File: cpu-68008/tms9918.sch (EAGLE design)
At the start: 45 parts, among them IC101 74HCT245, IC102 74HCT245, IC103 74HCT245, IC104 74HCT245, IC201 GAL22V10D

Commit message: added /DS to GALs on all peripherals and backplane began work on TMS9918 video card
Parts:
- removed C105, C107, C202, C301, C302, C303, C304: 100nF, rcl:C-EUC0805
- removed C106, C201, C305, C306: 10µF, rcl:CPOL-EUSMCB
- removed H101, H102, H103, H104: MOUNT-HOLE2.8, holes:MOUNT-HOLE2.8
- removed IC102, IC103, IC104: 74HCT245, 74xx-eu:74HCT245DW
- removed IC201: GAL22V10D, 68komputer:GAL22V10DIP24
- removed LED101, LED301, LED302, LED303, LED304: (no value), led:LEDCHIPLED_1206
- removed R101, R102: 10k, rcl:R-EU_R2012
- removed R103, R301, R302, R303, R304: 3k, rcl:R-EU_R2012
- removed SV102: (no value), con-lstb:MA20-2
- removed SV103: (no value), con-lstb:MA10-2W
- removed SV104: (no value), con-lstb:MA20-2W
- removed SV301, SV302, SV303, SV304: (no value), con-lsta:FE20-2
- removed WEED301: WEED, 68komputer:WEED
- added C1, C6: 10µF, rcl:CPOL-EUSMCB
- added C2, C3, C4, C5, C7: 100nF, rcl:C-EUC0805
- added IC1, IC2, IC3: 74HCT574N, 74xx-eu:74HCT574N
- added IC4: 74HCT04N, 74xx-eu:74HCT04N
- added IC5: AS6C62256, 68komputer:AS6C62256
- added LED201: (no value), led:LEDCHIPLED_1206
- added R201: 10k, rcl:R-EU_R2012
- added R202: 3k, rcl:R-EU_R2012
- C102: value 47µF -> 10µF; device rcl:CPOL-EUE2-5 -> rcl:CPOL-EUSMCB; MOUSER 710-860020472006 -> 581-TAJB106K020RNJV
- C104: value 100nF -> 10µF; device rcl:C-EUC0805 -> rcl:CPOL-EUSMCB; MOUSER 710-885012207072 -> 581-TAJB106K020RNJV
- IC101: value 74HCT245 -> GAL22V10D; device 74xx-eu:74HCT245DW -> 68komputer:GAL22V10DIP24; MOUSER_SOCKET (none) -> 575-11044324
- SV101: device con-lstb:MA10-2 -> con-lstb:MA20-2W
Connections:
- removed net !AS: IC104A.A1, SV102.33, SV104.33
- removed net !BERR: SV102.9, SV104.9
- removed net !BG: SV102.25, SV104.25
- removed net !BR: SV102.23, SV104.23
- removed net !BUF_ADDR_OE: IC102A.G, IC103A.G, IC201.IO17
- removed net !BUF_DATA_OE: IC101A.G, IC201.IO16
- removed net !BUS_CS: IC201.IN2, SV101.7, SV103.7
- removed net !BUS_DTACK: IC201.IO14, SV101.6, SV103.6
- removed net !DS: IC104A.A2, SV102.31, SV104.31
- removed net !DTACK: SV102.27, SV104.27
- removed net !HALT: SV102.17, SV104.17
- removed net !RESET: IC104A.A8, SV102.15, SV104.15
- removed net !SLOT_CS0: IC201.IO23, LED301.C, SV301.5
- removed net !SLOT_CS1: IC201.IO22, LED302.C, SV303.5
- removed net !SLOT_CS2: IC201.IO21, LED303.C, SV302.5
- removed net !SLOT_CS3: IC201.IO20, LED304.C, SV304.5
- removed net !VPA: SV102.11, SV104.11
- removed net A0: IC102A.A4, SV101.17, SV103.17
- removed net A1: IC102A.A6, SV101.15, SV103.15
- removed net A10: IC103A.A6, SV102.8, SV104.8
- removed net A11: IC103A.A5, SV102.10, SV104.10
- removed net A12: IC103A.A4, SV102.12, SV104.12
- removed net A13: IC103A.A3, SV102.14, SV104.14
- removed net A14: IC103A.A2, SV102.16, SV104.16
- removed net A15: IC103A.A1, SV102.20, SV104.20
- removed net A16: IC104A.A7, SV102.24, SV104.24
- removed net A17: IC104A.A6, SV102.26, SV104.26
- removed net A18: IC104A.A5, SV102.28, SV104.28
- removed net A19: IC104A.A3, SV102.30, SV104.30
- removed net A2: IC102A.A8, SV101.13, SV103.13
- removed net A3: IC102A.A7, SV101.14, SV103.14
- removed net A4: IC102A.A5, SV101.16, SV103.16
- removed net A5: IC102A.A3, SV101.18, SV103.18
- removed net A6: IC102A.A2, SV101.20, SV103.20
- removed net A7: IC102A.A1, SV102.2, SV104.2
- removed net A8: IC103A.A8, SV102.4, SV104.4
- removed net A9: IC103A.A7, SV102.6, SV104.6
- removed net BUF_DATA_DIR: IC101A.DIR, IC201.IO15
- removed net CLK: IC201.IN1/CLK, SV102.21, SV104.21
- removed net D0: IC101A.A6, SV102.35, SV104.35
- removed net D1: IC101A.A4, SV102.37, SV104.37
- removed net D2: IC101A.A2, SV102.39, SV104.39
- removed net D3: IC101A.A1, SV102.40, SV104.40
- removed net D4: IC101A.A3, SV102.38, SV104.38
- removed net D5: IC101A.A5, SV102.36, SV104.36
- removed net D6: IC101A.A7, SV102.34, SV104.34
- removed net D7: IC101A.A8, SV102.32, SV104.32
- removed net E: SV102.13, SV104.13
- removed net FC0: SV101.19, SV103.19
- removed net FC1: SV102.1, SV104.1
- removed net FC2: SV102.3, SV104.3
- removed net N$14: IC201.IN10
- removed net N$15: IC201.IN11
- removed net N$20: IC201.IO19
- removed net N$27: IC201.IO18
- removed net N$3: LED304.A, R304.2
- removed net N$4: LED101.A, R103.2
- removed net N$5: LED303.A, R303.2
- removed net R/!W!: IC104A.A4, SV102.29, SV104.29
- removed net SLOT_A16: IC104A.B7, IC201.IN3
- removed net SLOT_A17: IC104A.B6, IC201.IN4
- removed net SLOT_A18: IC104A.B5, IC201.IN5
- removed net SLOT_A19: IC104A.B3, IC201.IN7
- new net !ATA_ACTY: LED201.C
- new net !ATA_IRQ: R201.1
- new net !SLOT_CS: IC101.IN13, SV101.5
- new net !TMS_CAS: IC4C.I, IC5.!CS
- new net !TMS_RAS: IC4B.I
- new net !TMS_RD: IC1A.CLK, IC4A.O, IC4F.I, IC5.!OE
- new net !TMS_WR: IC4F.O
- new net COL: IC3A.CLK, IC4E.O
- new net N$7: LED201.A, R202.2
- new net ROW: IC2A.CLK, IC4B.O
- new net TMS_AD0: IC1A.1D, IC2A.1D, IC3A.1D
- new net TMS_AD1: IC1A.2D, IC2A.2D, IC3A.2D
- new net TMS_AD2: IC1A.3D, IC2A.3D, IC3A.3D
- new net TMS_AD3: IC1A.4D, IC2A.4D, IC3A.4D
- new net TMS_AD4: IC1A.5D, IC2A.5D, IC3A.5D
- new net TMS_AD5: IC1A.6D, IC2A.6D, IC3A.6D
- new net TMS_AD6: IC1A.7D, IC2A.7D, IC3A.7D
- new net TMS_AD7: IC1A.8D, IC2A.8D, IC3A.8D
- new net TMS_R/!W!: IC1A.OC, IC4A.I, IC5.!WE
- new net TMS_VD0: IC1A.1Q, IC5.DQ0
- new net TMS_VD1: IC1A.2Q, IC5.DQ1
- new net TMS_VD2: IC1A.3Q, IC5.DQ2
- new net TMS_VD3: IC1A.4Q, IC5.DQ3
- new net TMS_VD4: IC1A.5Q, IC5.DQ4
- new net TMS_VD5: IC1A.6Q, IC5.DQ5
- new net TMS_VD6: IC1A.7Q, IC5.DQ6
- new net TMS_VD7: IC1A.8Q, IC5.DQ7
- new net VRAM_A0: IC2A.2Q, IC5.A0
- new net VRAM_A1: IC2A.3Q, IC5.A1
- new net VRAM_A10: IC3A.5Q, IC5.A10
- new net VRAM_A11: IC3A.6Q, IC5.A11
- new net VRAM_A12: IC3A.7Q, IC5.A12
- new net VRAM_A13: IC3A.8Q, IC5.A13
- new net VRAM_A2: IC2A.4Q, IC5.A2
- new net VRAM_A3: IC2A.5Q, IC5.A3
- new net VRAM_A4: IC2A.6Q, IC5.A4
- new net VRAM_A5: IC2A.7Q, IC5.A5
- new net VRAM_A6: IC2A.8Q, IC5.A6
- new net VRAM_A7: IC3A.2Q, IC5.A7
- new net VRAM_A8: IC3A.3Q, IC5.A8
- new net VRAM_A9: IC3A.4Q, IC5.A9
- new net VRAM_BANK: IC5.A14
- net !BUS_IRQ: now also IC101.IO15, SV101.6; no longer R101.1, SV101.5, SV103.5, SV301.6, SV302.6, SV303.6, SV304.6
- net !SLOT_ACK: now also IC101.IO14, SV101.24; no longer IC201.IN13, R102.1, SV301.24, SV302.24, SV303.24, SV304.24
- net !SLOT_AS: now also IC101.IN7, SV101.32; no longer IC104A.B1, SV301.32, SV302.32, SV303.32, SV304.32
- net !SLOT_DS: now also IC101.IN6, SV101.31; no longer IC104A.B2, IC201.IN9, SV301.31, SV302.31, SV303.31, SV304.31
- net !SLOT_RESET: now also IC101.IN8, SV101.30; no longer IC104A.B8, IC201.IN8, SV301.30, SV302.30, SV303.30, SV304.30
- net +5V: now also C1.+, C104.+, C2.1, C3.1, C4.1, C5.1, C6.+, C7.1, IC101.VCC, IC1P.VCC, IC2P.VCC, IC3P.VCC, IC4P.VCC, IC5.VCC, R201.2, R202.1; no longer C104.1, C105.1, C106.+, C107.1, C201.+, C202.1, C301.1, C302.1, C303.1, C304.1, C305.+, C306.+, IC101P.VCC, IC102A.DIR, IC102P.VCC, IC103A.DIR, IC103P.VCC, IC104A.DIR, IC104P.VCC, IC201.VCC, R101.2, R102.2, R103.1, R301.1, R302.1, R303.1, R304.1, SV103.1, SV103.2, SV301.1, SV301.2, SV302.1, SV302.2, SV303.1, SV303.2, SV304.1, SV304.2
- net GND: now also C1.-, C104.-, C2.2, C3.2, C4.2, C5.2, C6.-, C7.2, IC101.GND, IC1P.GND, IC2A.OC, IC2P.GND, IC3A.OC, IC3P.GND, IC4P.GND, IC5.GND, SV101.25, SV101.26, SV101.27, SV101.28; no longer C104.2, C105.2, C106.-, C107.2, C201.-, C202.2, C301.2, C302.2, C303.2, C304.2, C305.-, C306.-, IC101P.GND, IC102P.GND, IC103P.GND, IC104A.G, IC104P.GND, IC201.GND, LED101.C, SV101.10, SV101.11, SV101.12, SV101.8, SV101.9, SV102.18, SV102.19, SV102.22, SV102.5, SV102.7, SV103.10, SV103.11, SV103.12, SV103.3, SV103.4, SV103.8, SV103.9, SV104.18, SV104.19, SV104.22, SV104.5, SV104.7, SV301.25, SV301.26, SV301.27, SV301.28, SV301.3, SV301.4, SV302.25, SV302.26, SV302.27, SV302.28, SV302.3, SV302.4, SV303.25, SV303.26, SV303.27, SV303.28, SV303.3, SV303.4, SV304.25, SV304.26, SV304.27, SV304.28, SV304.3, SV304.4
- net N$1: now also IC4D.O, IC4E.I; no longer LED302.A, R302.2
- net N$2: now also IC4C.O, IC4D.I; no longer LED301.A, R301.2
- net SLOT_A0: now also SV101.12; no longer IC102A.B4, SV301.12, SV302.12, SV303.12, SV304.12
- net SLOT_A1: now also SV101.10; no longer IC102A.B6, SV301.10, SV302.10, SV303.10, SV304.10
- net SLOT_A10: now also SV101.18; no longer IC103A.B6, SV301.18, SV302.18, SV303.18, SV304.18
- net SLOT_A11: now also SV101.17; no longer IC103A.B5, SV301.17, SV302.17, SV303.17, SV304.17
- net SLOT_A12: now also SV101.20; no longer IC103A.B4, SV301.20, SV302.20, SV303.20, SV304.20
- net SLOT_A13: now also SV101.19; no longer IC103A.B3, SV301.19, SV302.19, SV303.19, SV304.19
- net SLOT_A14: now also SV101.22; no longer IC103A.B2, SV301.22, SV302.22, SV303.22, SV304.22
- net SLOT_A15: now also SV101.21; no longer IC103A.B1, SV301.21, SV302.21, SV303.21, SV304.21
- net SLOT_A2: now also SV101.8; no longer IC102A.B8, SV301.8, SV302.8, SV303.8, SV304.8
- net SLOT_A3: now also SV101.7; no longer IC102A.B7, SV301.7, SV302.7, SV303.7, SV304.7
- net SLOT_A4: now also IC101.IN10, SV101.9; no longer IC102A.B5, SV301.9, SV302.9, SV303.9, SV304.9
- net SLOT_A5: now also IC101.IN11, SV101.11; no longer IC102A.B3, SV301.11, SV302.11, SV303.11, SV304.11
- net SLOT_A6: now also SV101.14; no longer IC102A.B2, SV301.14, SV302.14, SV303.14, SV304.14
- net SLOT_A7: now also SV101.13; no longer IC102A.B1, SV301.13, SV302.13, SV303.13, SV304.13
- net SLOT_A8: now also SV101.16; no longer IC103A.B8, SV301.16, SV302.16, SV303.16, SV304.16
- net SLOT_A9: now also SV101.15; no longer IC103A.B7, SV301.15, SV302.15, SV303.15, SV304.15
- net SLOT_D0: now also SV101.35; no longer IC101A.B6, SV301.35, SV302.35, SV303.35, SV304.35
- net SLOT_D1: now also SV101.37; no longer IC101A.B4, SV301.37, SV302.37, SV303.37, SV304.37
- net SLOT_D2: now also SV101.39; no longer IC101A.B2, SV301.39, SV302.39, SV303.39, SV304.39
- net SLOT_D3: now also SV101.40; no longer IC101A.B1, SV301.40, SV302.40, SV303.40, SV304.40
- net SLOT_D4: now also SV101.38; no longer IC101A.B3, SV301.38, SV302.38, SV303.38, SV304.38
- net SLOT_D5: now also SV101.36; no longer IC101A.B5, SV301.36, SV302.36, SV303.36, SV304.36
- net SLOT_D6: now also SV101.34; no longer IC101A.B7, SV301.34, SV302.34, SV303.34, SV304.34
- net SLOT_D7: now also SV101.33; no longer IC101A.B8, SV301.33, SV302.33, SV303.33, SV304.33
- net SLOT_R/!W!: now also IC101.IN9, SV101.23; no longer IC104A.B4, IC201.IN6, SV301.23, SV302.23, SV303.23, SV304.23
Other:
- note removed: "1x 100nF for each IC101-4 1x 10µF shared between IC101-4"
- note removed: "One 10µF per two slots"
- note removed: "SV103/104 are duplicated as SV101/102 for a logic analyzer to be attached"
- note removed: "Slot 1"
- note removed: "Slot 2"
- note removed: "Slot 3"
- note removed: "Slot 4"

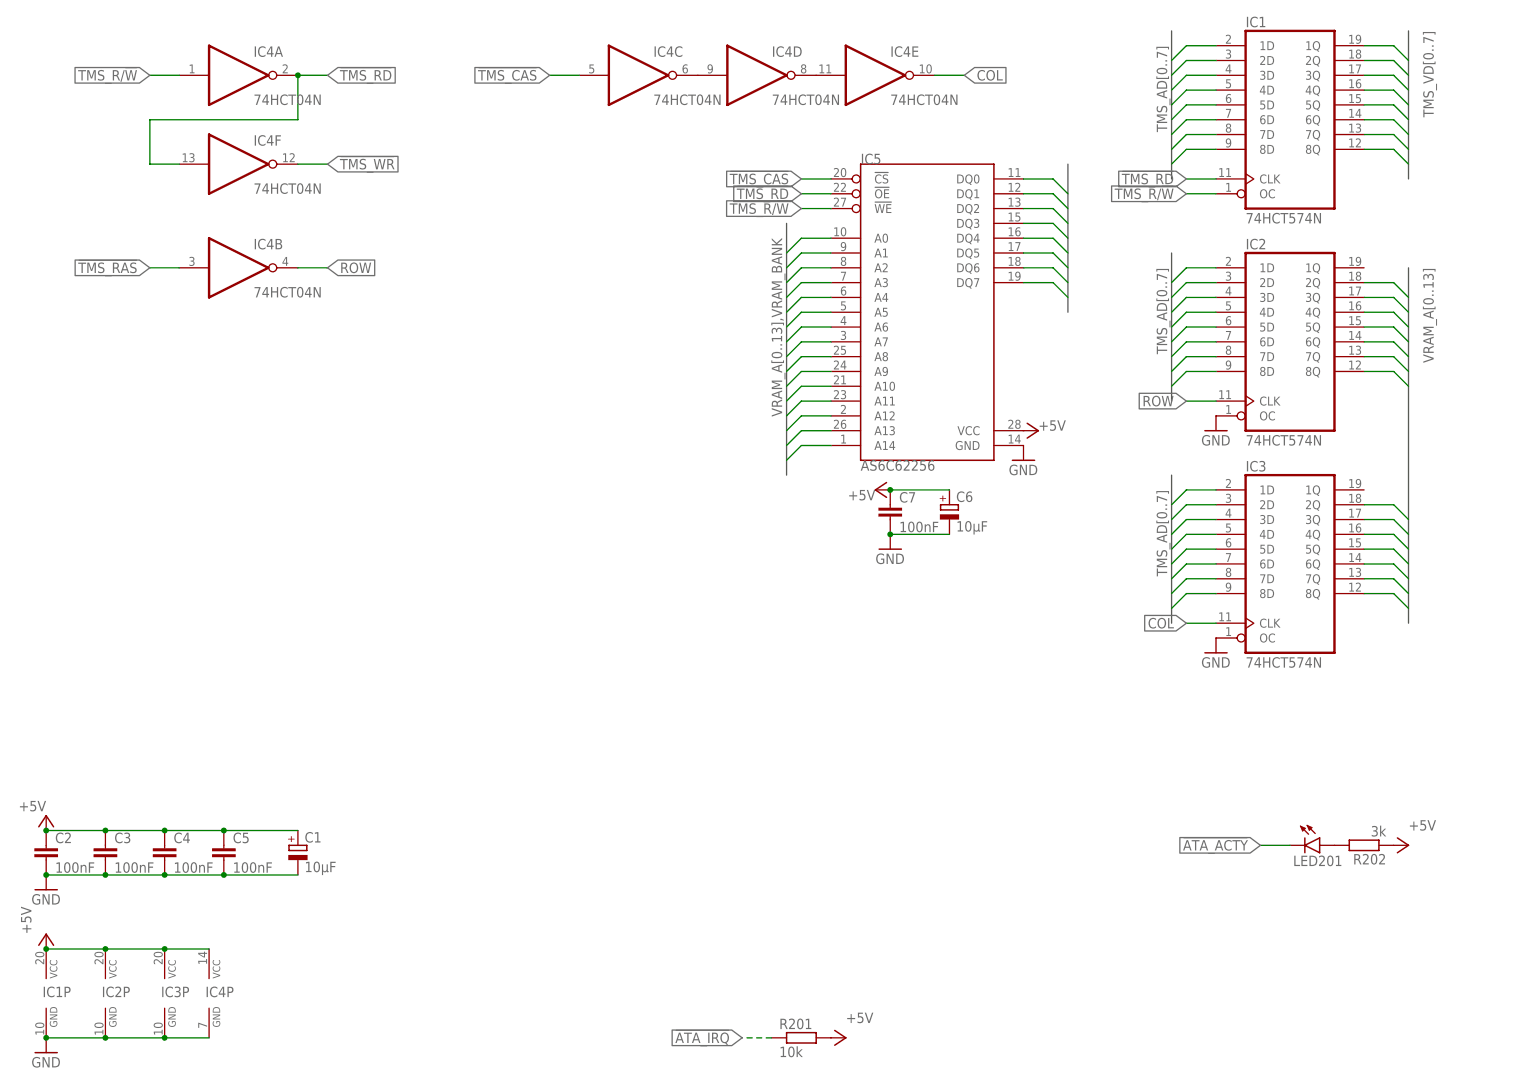
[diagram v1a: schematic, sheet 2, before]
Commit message: finished schematic for tms9918 board, started routing
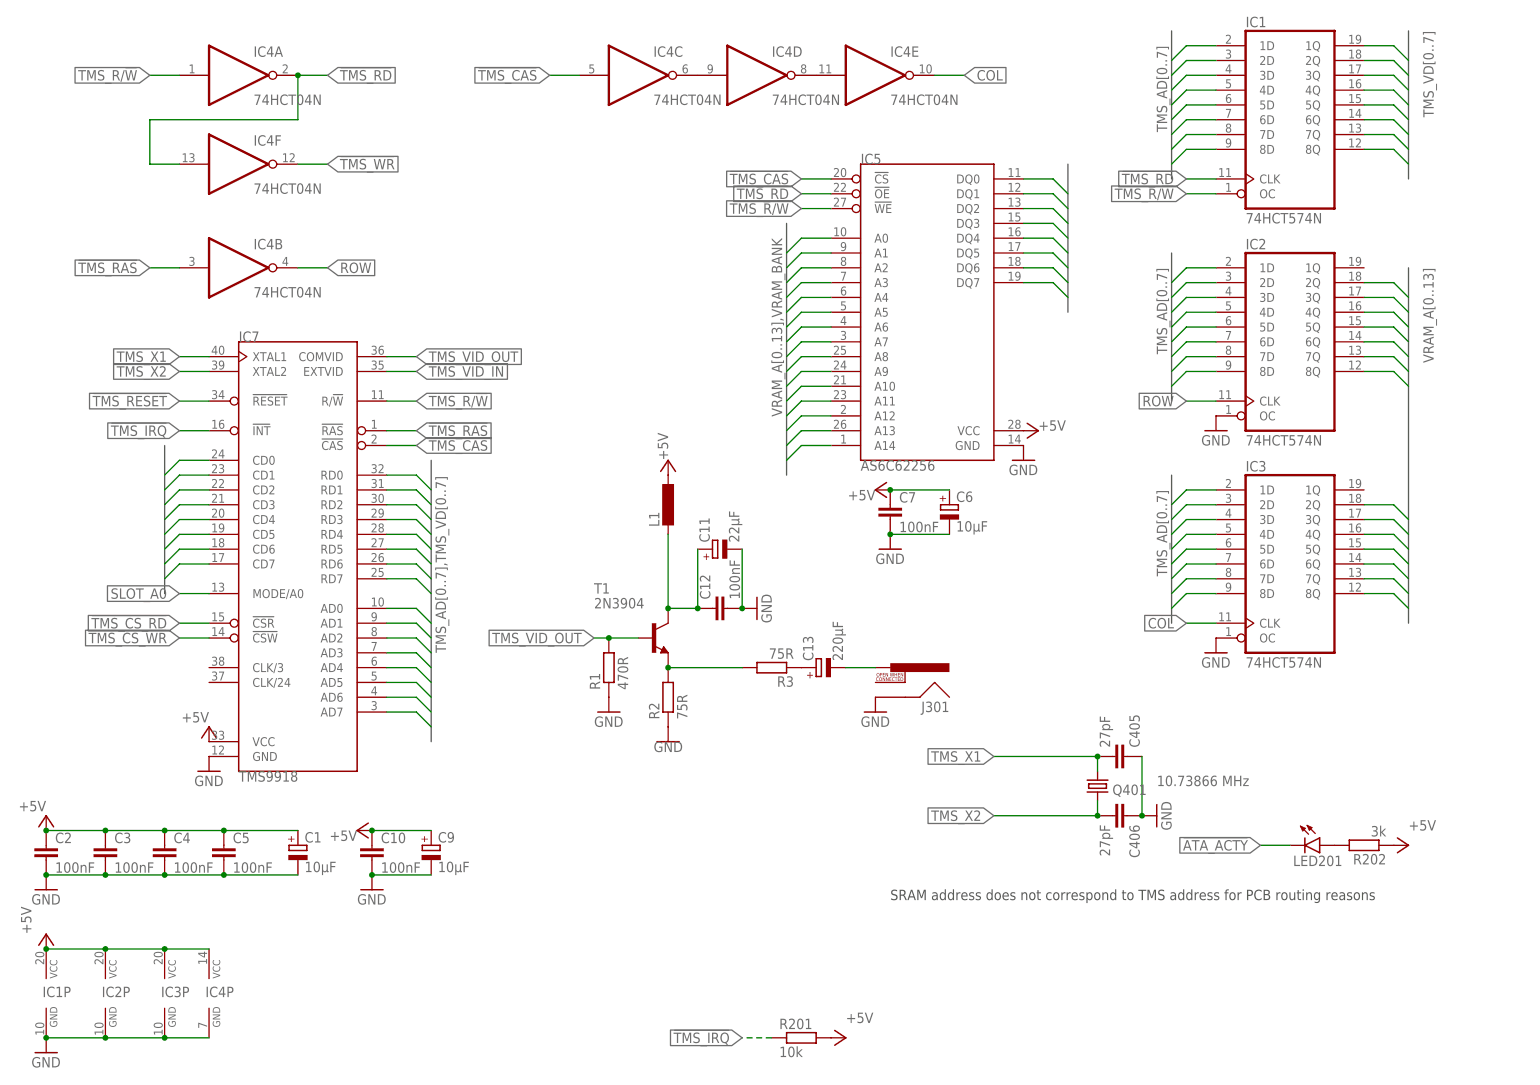
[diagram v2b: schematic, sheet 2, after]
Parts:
- added C10, C12, C8: 100nF, rcl:C-EUC0805
- added C11: 22µF, rcl:CPOL-EUE2-5
- added C13: 220µF, rcl:CPOL-EUE2.5-7
- added C405, C406: 27pF, rcl:C-EUC0805
- added C9: 10µF, rcl:CPOL-EUSMCB
- added IC6: 74HCT373N, 74xx-eu:74HCT373N
- added IC7: TMS9918, 68komputer:TMS9918
- added J301: RCALOCK, SparkFun-Connectors:RCALOCK
- added L1: (no value), rcl:L-EUL2012C
- added Q401: 10.73866 MHz, crystal:CRYSTALHC49S
- added R1: 470R, rcl:R-EU_R2012
- added R2, R3: 75R, rcl:R-EU_R2012
- added T1: 2N3904, transistor-neu-to92:2N3904
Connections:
- removed net !ATA_IRQ: R201.1
- new net !TMS_CS_RD: IC101.IO18, IC7.!CSR
- new net !TMS_CS_WR: IC101.IO17, IC7.!CSW
- new net !TMS_IRQ: IC101.IN5, IC7.!INT, R201.1
- new net !TMS_RESET: IC101.IO19, IC7.!RESET
- new net CONFIG_LATCH: IC101.IO16, IC6A.ENC
- new net N$3: C11.+, C12.1, L1.2, T1.C
- new net N$4: R2.2, R3.2, T1.E
- new net N$5: C13.+, R3.1
- new net N$6: C13.-, J301.PIN
- new net TMS_VID_IN: IC7.EXTVID
- new net TMS_VID_OUT: IC7.COMVID, R1.2, T1.B
- new net TMS_X1: C405.2, IC7.XTAL1, Q401.1
- new net TMS_X2: C406.2, IC7.XTAL2, Q401.2
- new net VDP_RESET: IC101.IN6, IC6A.2Q
- net !BUS_IRQ: now also IC101.IO14; no longer IC101.IO15
- net !SLOT_ACK: now also IC101.IO15; no longer IC101.IO14
- net !SLOT_AS: now also IC101.IN8; no longer IC101.IN7
- net !SLOT_DS: now also IC101.IN7; no longer IC101.IN6
- net !SLOT_RESET: now also IC101.IN9; no longer IC101.IN8
- net !TMS_CAS: now also IC7.!CAS
- net !TMS_RAS: now also IC7.!RAS
- net +5V: now also C10.1, C8.1, C9.+, IC6P.VCC, IC7.VCC, L1.1
- net GND: now also C10.2, C11.-, C12.2, C405.1, C406.1, C8.2, C9.-, IC6A.3D, IC6A.4D, IC6A.5D, IC6A.6D, IC6A.7D, IC6A.8D, IC6A.OC, IC6P.GND, IC7.GND, J301.SHELL, R1.1, R2.1
- net SLOT_A0: now also IC7.MODE/A0
- net SLOT_A1: now also IC101.IN11
- net SLOT_A4: no longer IC101.IN10
- net SLOT_A5: no longer IC101.IN11
- net SLOT_D0: now also IC6A.1D, IC7.CD7
- net SLOT_D1: now also IC6A.2D, IC7.CD6
- net SLOT_D2: now also IC7.CD5
- net SLOT_D3: now also IC7.CD4
- net SLOT_D4: now also IC7.CD3
- net SLOT_D5: now also IC7.CD2
- net SLOT_D6: now also IC7.CD1
- net SLOT_D7: now also IC7.CD0
- net SLOT_R/!W!: now also IC101.IN10; no longer IC101.IN9
- net TMS_AD0: now also IC2A.8D, IC3A.8D, IC7.AD0; no longer IC2A.1D, IC3A.1D
- net TMS_AD1: now also IC2A.7D, IC3A.7D, IC7.AD1; no longer IC2A.2D, IC3A.2D
- net TMS_AD2: now also IC2A.6D, IC3A.6D, IC7.AD2; no longer IC2A.3D, IC3A.3D
- net TMS_AD3: now also IC2A.5D, IC3A.5D, IC7.AD3; no longer IC2A.4D, IC3A.4D
- net TMS_AD4: now also IC2A.4D, IC3A.4D, IC7.AD4; no longer IC2A.5D, IC3A.5D
- net TMS_AD5: now also IC2A.3D, IC3A.3D, IC7.AD5; no longer IC2A.6D, IC3A.6D
- net TMS_AD6: now also IC2A.2D, IC3A.2D, IC7.AD6; no longer IC2A.7D, IC3A.7D
- net TMS_AD7: now also IC2A.1D, IC3A.1D, IC7.AD7; no longer IC2A.8D, IC3A.8D
- net TMS_R/!W!: now also IC7.R/!W!
- net TMS_VD0: now also IC7.RD0
- net TMS_VD1: now also IC7.RD1
- net TMS_VD2: now also IC7.RD2
- net TMS_VD3: now also IC7.RD3
- net TMS_VD4: now also IC7.RD4
- net TMS_VD5: now also IC7.RD5
- net TMS_VD6: now also IC7.RD6
- net TMS_VD7: now also IC7.RD7
- net VRAM_A0: now also IC2A.8Q; no longer IC2A.2Q
- net VRAM_A1: now also IC2A.7Q; no longer IC2A.3Q
- net VRAM_A10: now also IC3A.8Q; no longer IC3A.5Q
- net VRAM_A11: now also IC3A.7Q; no longer IC3A.6Q
- net VRAM_A12: now also IC3A.2Q; no longer IC3A.7Q
- net VRAM_A13: now also IC3A.4Q; no longer IC3A.8Q
- net VRAM_A2: now also IC2A.6Q; no longer IC2A.4Q
- net VRAM_A4: now also IC2A.4Q; no longer IC2A.6Q
- net VRAM_A5: now also IC2A.3Q; no longer IC2A.7Q
- net VRAM_A6: now also IC2A.2Q; no longer IC2A.8Q
- net VRAM_A7: now also IC3A.3Q; no longer IC3A.2Q
- net VRAM_A8: now also IC3A.5Q; no longer IC3A.3Q
- net VRAM_A9: now also IC3A.6Q; no longer IC3A.4Q
- net VRAM_BANK: now also IC6A.1Q
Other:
- note added: "IC101 latches several control signals for the TMS9918"
- note added: "SRAM address does not correspond to TMS address for PCB routing reasons"
- moved on the sheet: C103, C104, IC101

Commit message: minor revisions on mouser parts
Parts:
- removed C6: 10µF, rcl:CPOL-EUSMCB
- removed C7, C8: 100nF, rcl:C-EUC0805
- removed R1: 470R, rcl:R-EU_R2012
- removed R2: 75R, rcl:R-EU_R2012
- added C105: 10µF, rcl:CPOL-EUSMCB
- added C106: 100nF, rcl:C-EUC0805
- added IC103: 74HCT175N, 74xx-eu:74HCT175N
- added LED101: (no value), led:LEDCHIPLED_1206
- added R101, R204: 3k, rcl:R-EU_R2012
- added R205: 10k, rcl:R-EU_R2012
- added SV102: (no value), con-lstb:MA05-2
- added WEED1: WEED, 68komputer:WEED
- C104: value 10µF -> 100nF; device rcl:CPOL-EUSMCB -> rcl:C-EUC0805; MOUSER 581-TAJB106K020RNJV -> 710-885012207072
- J201: MOUSER 502-PJRAN1X1U03AUX -> 502-PJRAN1X1U04AU
- R201: value 10k -> 470R; MOUSER 652-CR0805FX-1002ELF -> 652-CR0805FX-4700ELF
- R202: value 3k -> 75R; MOUSER 652-CR0805JW-302ELF -> 652-CR0805FX-75R0ELF
- renumbered C1 to C205, C10 to C206, C11 to C208, C12 to C209, C13 to C210, C2 to C201, C3 to C202, C4 to C203, C405 to C211, C406 to C212, C5 to C204, C9 to C207, IC1 to IC204, IC2 to IC205, IC3 to IC206, IC4 to IC201, IC5 to IC203, IC6 to IC102, IC7 to IC202, J301 to J201, L1 to L201, Q401 to Q201, R3 to R203, T1 to T201
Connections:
- removed net !ATA_ACTY: LED201.C
- new net !ACCESS_TIMER_CLEAR: IC101.IN2, IC103A.CLR
- new net !DONE_1: IC103A.!Q1, SV102.10
- new net !DONE_2: IC103A.!Q2, SV102.8
- new net !DONE_3: IC103A.!Q3, SV102.6
- new net !DONE_4: IC103A.!Q4, SV102.4
- new net !TMS_DONE: IC101.IN3, SV102.1, SV102.3, SV102.5, SV102.7, SV102.9
- new net N$10: IC103A.D4, IC103A.Q3
- new net N$11: LED101.A, R101.2
- new net N$8: IC103A.D2, IC103A.Q1
- new net N$9: IC103A.D3, IC103A.Q2
- new net TMS_CLK24: IC202.CLK/24
- new net TMS_CLK3: IC103A.CLK, IC202.CLK/3
- net !TMS_IRQ: now also LED201.C, R205.1; no longer R201.1
- net +5V: now also C104.1, C105.+, C106.1, IC103A.D1, IC103P.VCC, R204.1, R205.2; no longer C104.+, C6.+, C7.1, C8.1, R201.2, R202.1
- net GND: now also C104.2, C105.-, C106.2, IC103P.GND, LED101.C, R201.1, R202.1, SV102.2; no longer C104.-, C6.-, C7.2, C8.2, R1.1, R2.1
- net N$4: now also R202.2; no longer R2.2
- net N$7: now also R204.2; no longer R202.2
- net TMS_VID_OUT: now also R201.2; no longer R1.2
- net VRAM_BANK: now also R101.1
